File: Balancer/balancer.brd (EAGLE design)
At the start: 170 x 230 mm, 303 parts, among them Q1 BSS123W, Q10A SIR882DP-T1-GE3, Q10B SIS468DN-T1-GE3, Q11A SIR882DP-T1-GE3, Q11B SIS468DN-T1-GE3, Q12A SIR882DP-T1-GE3, Q12B SIS468DN-T1-GE3, Q1A8 SIR882DP-T1-GE3, Q1B8 SIS468DN-T1-GE3, Q2 BSS123W, Q3A SIR882DP-T1-GE3, Q3B SIS468DN-T1-GE3, Q4 MMBT3906LT1G, Q4A SIR882DP-T1-GE3, Q4B SIS468DN-T1-GE3, Q5 FDN5618P, Q5A SIR882DP-T1-GE3, Q5B SIS468DN-T1-GE3, Q6 CMPT3904E_TR_PBFREE, Q6A SIR882DP-T1-GE3, Q6B SIS468DN-T1-GE3, Q9A SIR882DP-T1-GE3, Q9B SIS468DN-T1-GE3, T10 750312504, T11 750312504, T12 750312504, T3 750312504, T4 750312504, T5 750312504, T6 750312504, T8 750312504, T9 750312504, U1 LTC3300ILXE-1PBF, U2 LTC3300ILXE-1PBF

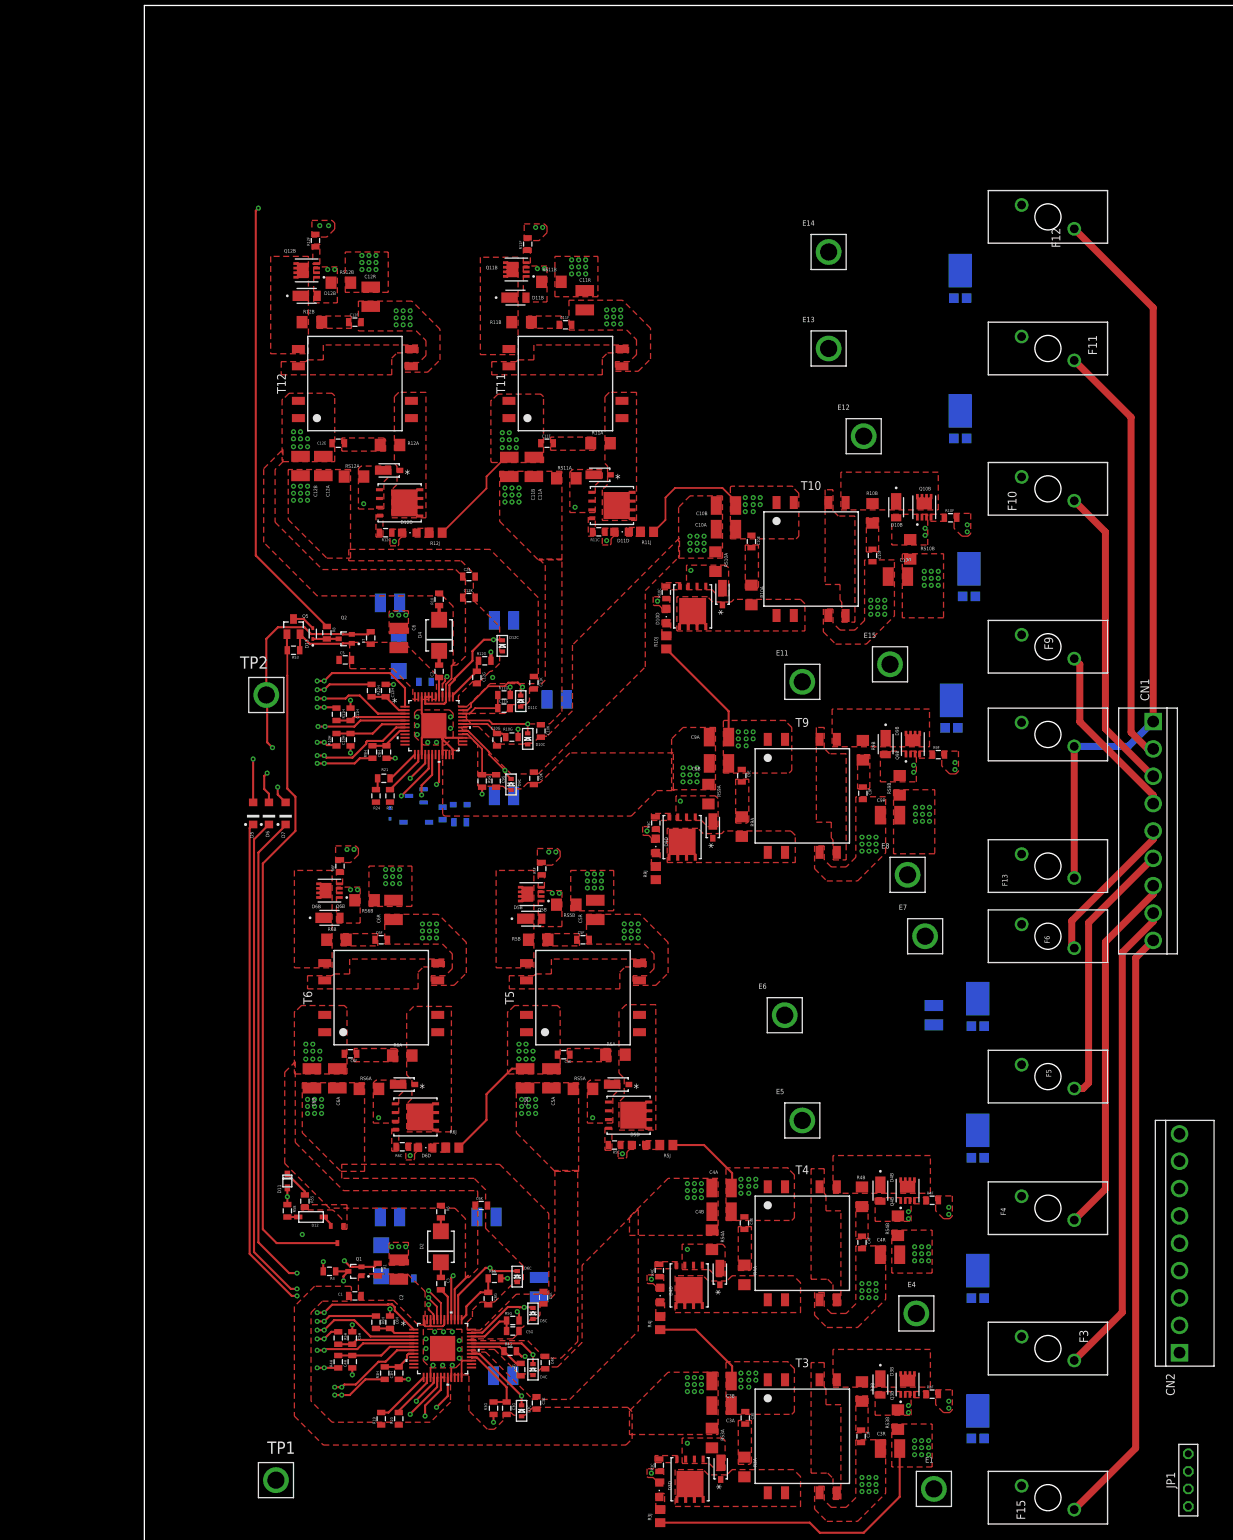
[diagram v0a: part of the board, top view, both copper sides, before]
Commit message: finished L3 and get half of L4 done
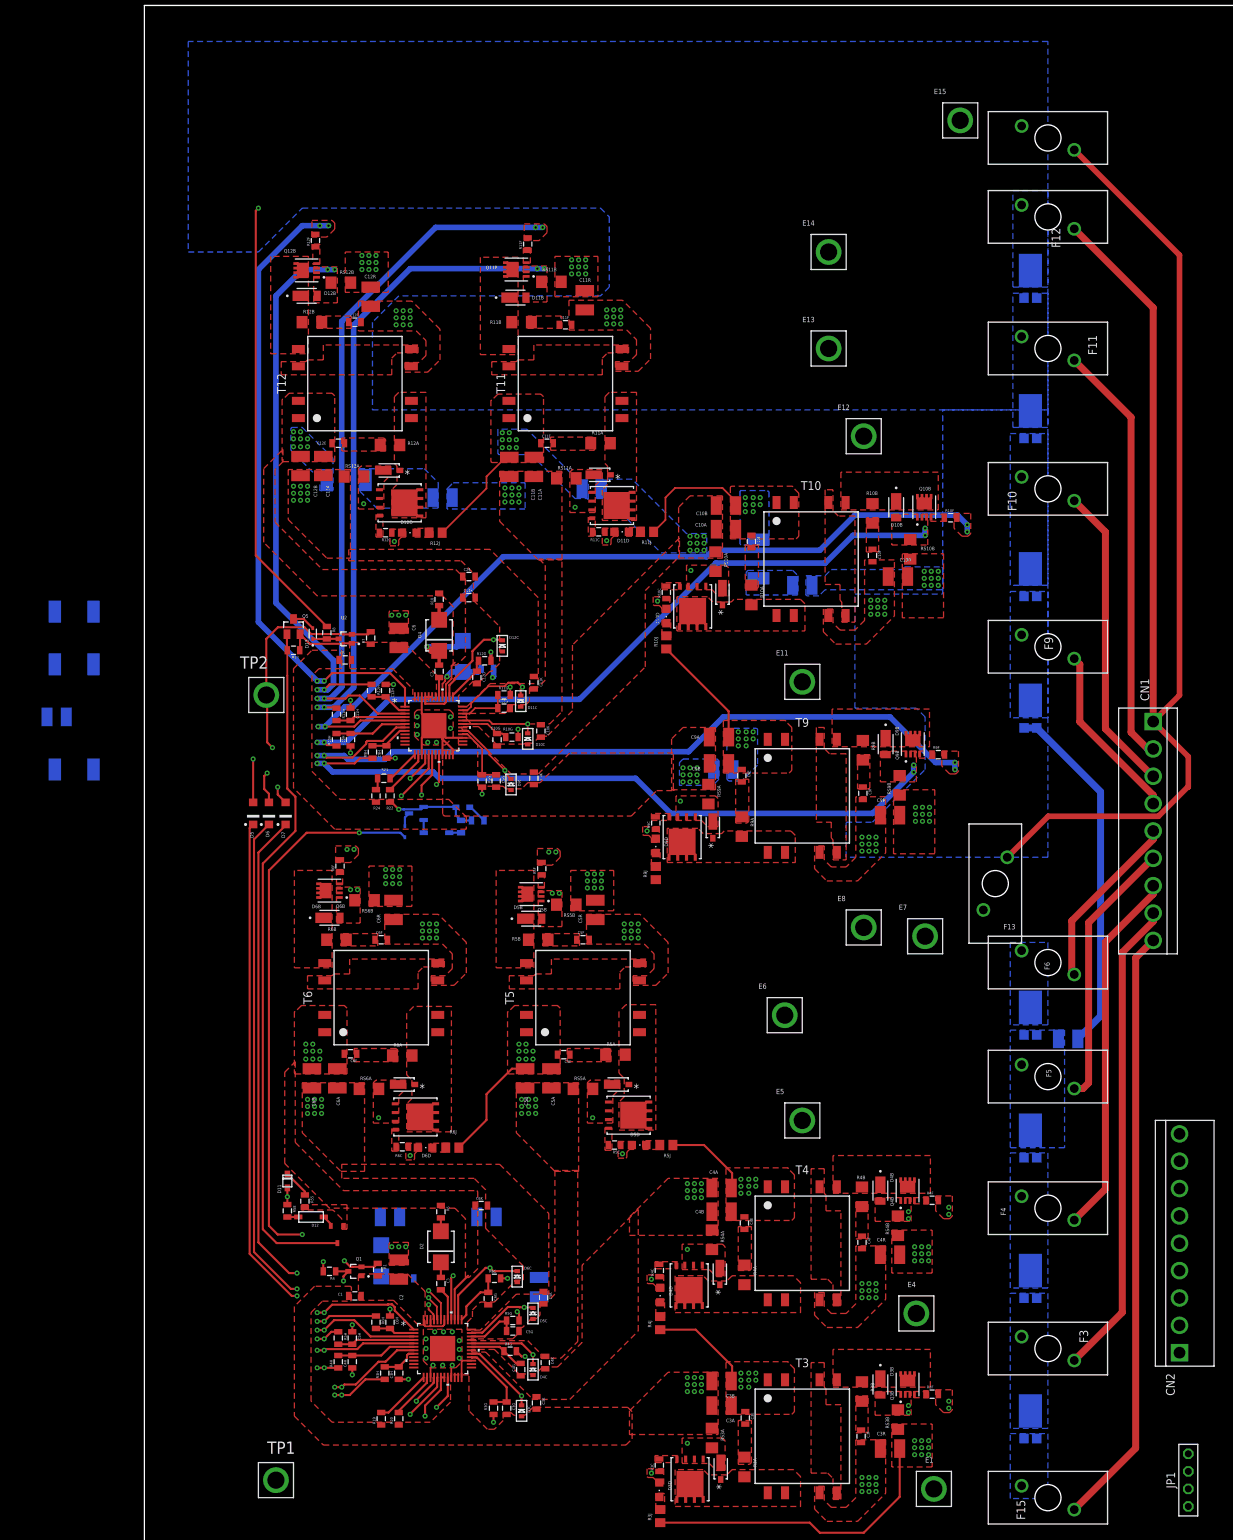
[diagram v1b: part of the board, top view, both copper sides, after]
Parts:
- added R11, R12, R13, R15, R16: 0, rcl:R2512
- moved C12 115.2 mm to (-12.7, 127.0)
- moved F14 86.4 mm to (130.8, 210.8)
- moved E15 79.4 mm to (118.1, 213.4)
- moved C17 39.2 mm to (95.2, 146.1), turned to 180 degrees
- moved C18 32.0 mm to (83.8, 119.4)
- moved C16 22.9 mm to (64.8, 160.0), turned to 180 degrees
- moved C13 19.7 mm to (133.7, 80.4), turned to 0 degrees
- moved C15 17.0 mm to (43.2, 158.8), turned to 180 degrees
- moved D9E 11.4 mm to (128.3, 128.3)
- moved D11E 10.2 mm to (128.3, 170.2)
- moved D12E 10.2 mm to (128.3, 190.5)
- moved E8 9.92 mm to (104.1, 96.5)
- moved D3 9.27 mm to (46.1, 135.8)
- moved C8 9.22 mm to (49.7, 134.0), turned to 180 degrees
- moved D10E 8.89 mm to (128.3, 147.3)
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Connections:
- net N$78 renamed C
- removed net C7: R54.1, R56.1
- new net N$66: C9.1, R11.1
- new net N$69: C11.1, R12.1
- new net N$71: C12.1, R13.1
- new net N$76: C15.1, R15.1
- new net N$92: C17.1, R16.1
- net C10: now also R16.2; no longer C17.1
- net C12: now also R15.2; no longer C15.1
- net C3: now also R13.2; no longer C12.1
- net C4: now also R12.2; no longer C11.1
- net C6: now also R11.2, R54.1, R56.1; no longer C9.1
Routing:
- net G10S: track 12.9 -> 120.2 mm
- net BAT+: track 108.0 -> 208.7 mm
- net N$100: track 3.01 -> 103.4 mm
- net G9S: track 14.8 -> 112.6 mm
- net N$84: track 8.31 -> 100.1 mm
- net G11S: track 14.0 -> 104.9 mm
- net N$116: track 2.84 -> 91.7 mm
- net N$5: track 17.0 -> 96.0 mm, vias 2 -> 3
- net G12S: track 16.8 -> 92.7 mm
- net N$132: track 8.19 -> 79.6 mm
- net C6: track 87.9 -> 150.0 mm, vias 67 -> 68
- net N$46: track 2.06 -> 9.64 mm, vias 0 -> 1
- net N$135: track 3.21 -> 8.62 mm
- net N$23: track 22.0 -> 25.8 mm
- net N$7: track 0.00 -> 2.85 mm
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- added copper zone on layer 16, net C10
- added copper zone on layer 16, net C11
- added copper zone on layer 16, net C12
- added copper zone on layer 16, net C3
- added copper zone on layer 16, net C4
- added copper zone on layer 16, net C5
- added copper zone on layer 16, net C6
- added copper zone on layer 16, net C9
- added copper zone on layer 16, net N$76
- added copper zone on layer 16, net N$92
- added copper zone on layer 16, net TOP6_TS
- added copper zone on layer 16, net V-

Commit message: Finished PCB drawing
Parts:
- removed C1A8, C1B8: 100uF, rcl:C1210
- removed C1E8, C1F8, C1H8: 470pF, Ilya_Teach:0805
- removed C1G8: 2.2nF, Ilya_Teach:0805
- removed C1R8: 2.2uF, rcl:C1210
- removed D1A8: DFLS260Q-7, balancer:SDO_POWERDI123_DIO
- removed D1B8: DFLS1100-7, DFLS1100-7:DIO_DFLS1100-7
- removed D1C8: (no value), adafruit:SOD-523
- removed D8E: SBR10U200P5, balancer:POWERDI5
- removed Q1A8: SIR882DP-T1-GE3, balancer:POWERPAK_SO-8_SINGLE_VIS
- removed Q1B8: SIS468DN-T1-GE3, SIS892DN:VISHAY_SIS468DN-T1-GE3
- removed R13: 0, rcl:R2512
- removed R1A8, R1B8: 20, rcl:R1206
- removed R1C8, R1F8: 5.1, Ilya_Teach:0805
- removed R1G8, R1H8: 20, Ilya_Teach:0805
- removed RS1A8: 0.005, rcl:R1206
- removed RS1B8: 0.01, rcl:R1206
- removed T8: 750312504, 750312504:WE-FLYLT_EP13_2381
- moved C12 132.5 mm to (81.8, 34.2)
- moved R12 130.5 mm to (87.6, 48.3), turned to 90 degrees
- moved R11 79.0 mm to (36.8, 78.7)
- moved C10 33.6 mm to (78.7, 71.1), turned to 270 degrees
- moved C11 23.2 mm to (79.6, 38.6)
- moved C9 19.4 mm to (45.7, 71.1), turned to 180 degrees
- moved D1 12.8 mm to (47.0, 47.0), turned to 90 degrees
- moved C4 12.0 mm to (49.5, 41.9), turned to 180 degrees
- moved C10R 0.38 mm to (109.1, 146.9)
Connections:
- removed net N$136: Q1A8.4, R1C8.2
- removed net N$137: D1C8.K, R1C8.1
- removed net N$138: C1A8.2, C1B8.2, C1G8.2, D1C8.A, D8E.P$2, D8E.P$3, RS1A8.1
- removed net N$139: C1E8.2, R1A8.1
- removed net N$140: C1A8.1, C1B8.1, C1E8.1, D8E.P$1, T8.1, T8.2
- removed net N$141: D1A8.1, Q1A8.5, Q1A8.6, Q1A8.7, Q1A8.8, Q1A8.9, R1A8.2, T8.10, T8.9
- removed net N$142: C1G8.1, R1G8.1
- removed net N$143: D1A8.2, Q1A8.1, Q1A8.2, Q1A8.3, R1G8.2, RS1A8.2
- removed net N$144: T8.4, T8.6
- removed net N$145: C1F8.1, R1B8.2
- removed net N$146: C1F8.2, C1R8.1, T8.7
- removed net N$147: D1B8.K, Q1B8.5, Q1B8.6, Q1B8.7, Q1B8.8, Q1B8.9, R1B8.1, T8.5
- removed net N$148: D1B8.A, Q1B8.1, Q1B8.2, Q1B8.3, R1H8.1, RS1B8.2
- removed net N$149: C1H8.2, R1H8.2
- removed net N$150: Q1B8.4, R1F8.1
- removed net N$151: R1F8.2
- removed net N$156: C1H8.1, C1R8.2, RS1B8.1
- removed net N$71: C12.1, R13.1
- net C3: now also C12.1; no longer R13.2
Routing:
- net G4S: track 14.4 -> 116.6 mm
- net N$36: track 3.05 -> 99.7 mm
- net G3S: track 13.7 -> 106.6 mm
- net G5S: track 15.6 -> 107.5 mm
- net N$20: track 8.18 -> 94.6 mm
- net N$52: track 3.47 -> 85.3 mm
- net G6S: track 16.3 -> 92.4 mm
- net N$68: track 8.83 -> 79.2 mm
- net C6: track 150.0 -> 204.6 mm
- net BOOST+: track 6.48 -> 12.8 mm
- net N$1: track 2.18 -> 8.09 mm, vias 0 -> 1
- net V-: track 102.7 -> 105.3 mm
- net C5: track 58.2 -> 59.7 mm, vias 18 -> 19
- added copper zone on layer 16, net BOT6_TS
- added copper zone on layer 1, net N$21
- added copper zone on layer 1, net N$38
- added copper zone on layer 16, net N$66
- added copper zone on layer 16, net N$69
- removed copper zone on layer 1, net N$110
- removed copper zone on layer 1, net N$87

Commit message: done final check, generated Gerber file
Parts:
- removed CN1, CN2: (no value), jst-vh:B9P-VH
- removed JP1: PINHD-1X4, Connector:1X04
- removed TP1, TP2: 2501-2-00-80-00-00-07-0, Turret:MILMAX_2501-2-00-80-00-00-07-0
- added BATT, VOLT_TAPS: (no value), jst-vh:B9P-VH
- added COMM: PINHD-1X4, Connector:1X04
- added WDTA, WDTC: 2501-2-00-80-00-00-07-0, Turret:MILMAX_2501-2-00-80-00-00-07-0
- moved D11E 10.5 mm to (118.1, 167.6)
- moved Q10B 10.5 mm to (102.7, 154.8)
- moved R16 10.5 mm to (78.7, 147.3)
- moved RS10A 10.5 mm to (72.5, 146.9)
- moved C3E 10.5 mm to (76.8, 23.0)
- moved D5E 10.5 mm to (118.1, 63.5)
- moved D9A 10.5 mm to (72.1, 108.5)
- moved D9E 10.5 mm to (118.1, 125.7)
- moved R4F 10.5 mm to (103.9, 54.5)
- moved R9B 10.5 mm to (93.9, 119.6)
- moved C11 10.5 mm to (69.5, 36.1)
- moved C9F 10.5 mm to (93.9, 113.4)
- moved D10E 10.5 mm to (118.1, 144.8)
- moved D12E 10.5 mm to (118.1, 188.0)
- moved D3D 10.5 mm to (64.4, 12.6)
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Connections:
- net BAT+: now also BATT.1; no longer CN1.1
- net C10: now also VOLT_TAPS.7; no longer CN2.7
- net C11: now also VOLT_TAPS.8; no longer CN2.8
- net C12: now also VOLT_TAPS.9; no longer CN2.9
- net C3: now also VOLT_TAPS.2; no longer CN2.2
- net C4: now also VOLT_TAPS.3; no longer CN2.3
- net C5: now also VOLT_TAPS.4; no longer CN2.4
- net C6: now also VOLT_TAPS.5; no longer CN2.5
- net C9: now also VOLT_TAPS.6; no longer CN2.6
- net CSBI: now also COMM.3; no longer JP1.3
- net N$14: now also BATT.2; no longer CN1.2
- net N$18: now also BATT.3; no longer CN1.3
- net N$22: now also BATT.4; no longer CN1.4
- net N$23: now also BATT.5; no longer CN1.5
- net N$25: now also BATT.6; no longer CN1.6
- net N$26: now also BATT.7; no longer CN1.7
- net N$28: now also BATT.8; no longer CN1.8
- net N$30: now also BATT.9; no longer CN1.9
- net SCKI: now also COMM.2; no longer JP1.2
- net SDIO: now also COMM.1; no longer JP1.1
- net V-: now also COMM.4, VOLT_TAPS.1; no longer CN2.1, JP1.4
- net WDTA: now also WDTA.1; no longer TP1.1
- net WDTC: now also WDTC.1; no longer TP2.1
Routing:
- net BAT+: track 208.7 -> 208.2 mm
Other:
- board size 170 x 230 mm -> 145 x 220 mm

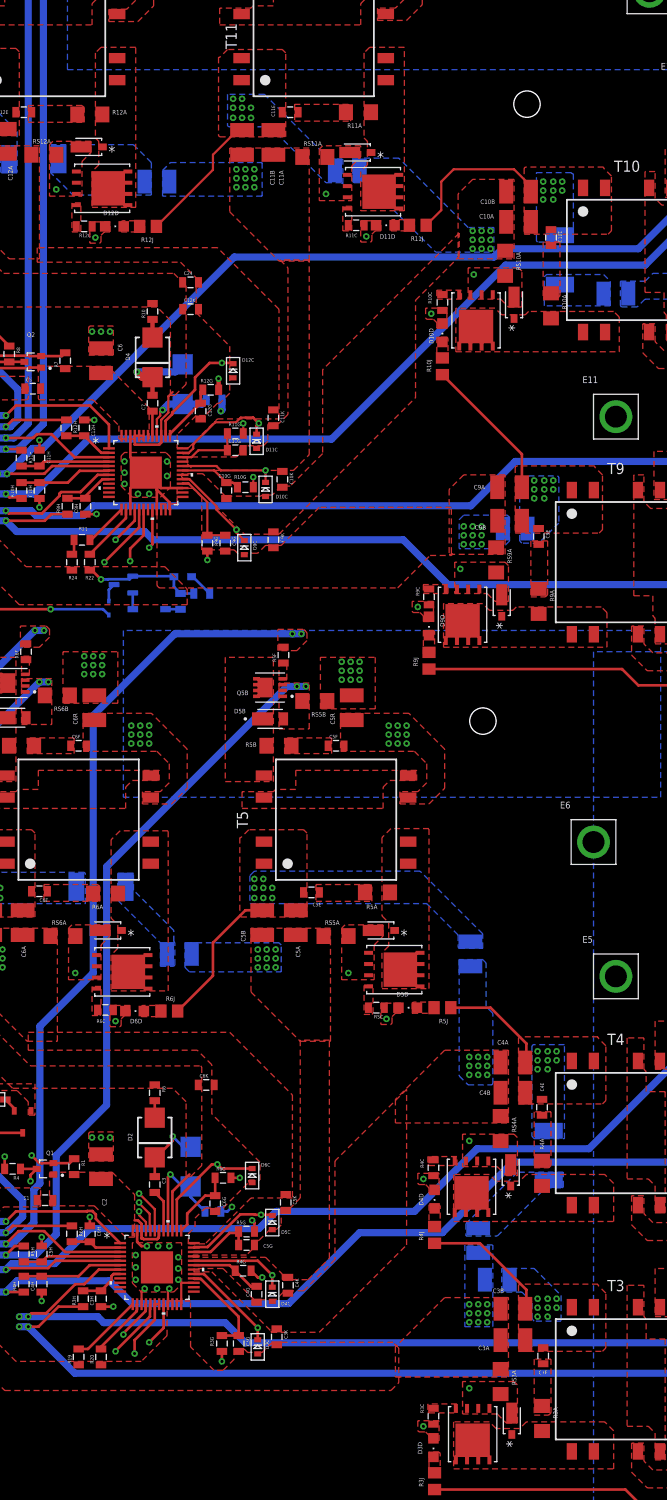
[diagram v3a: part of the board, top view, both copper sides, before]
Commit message: fixed wrong library on D3A-D12A
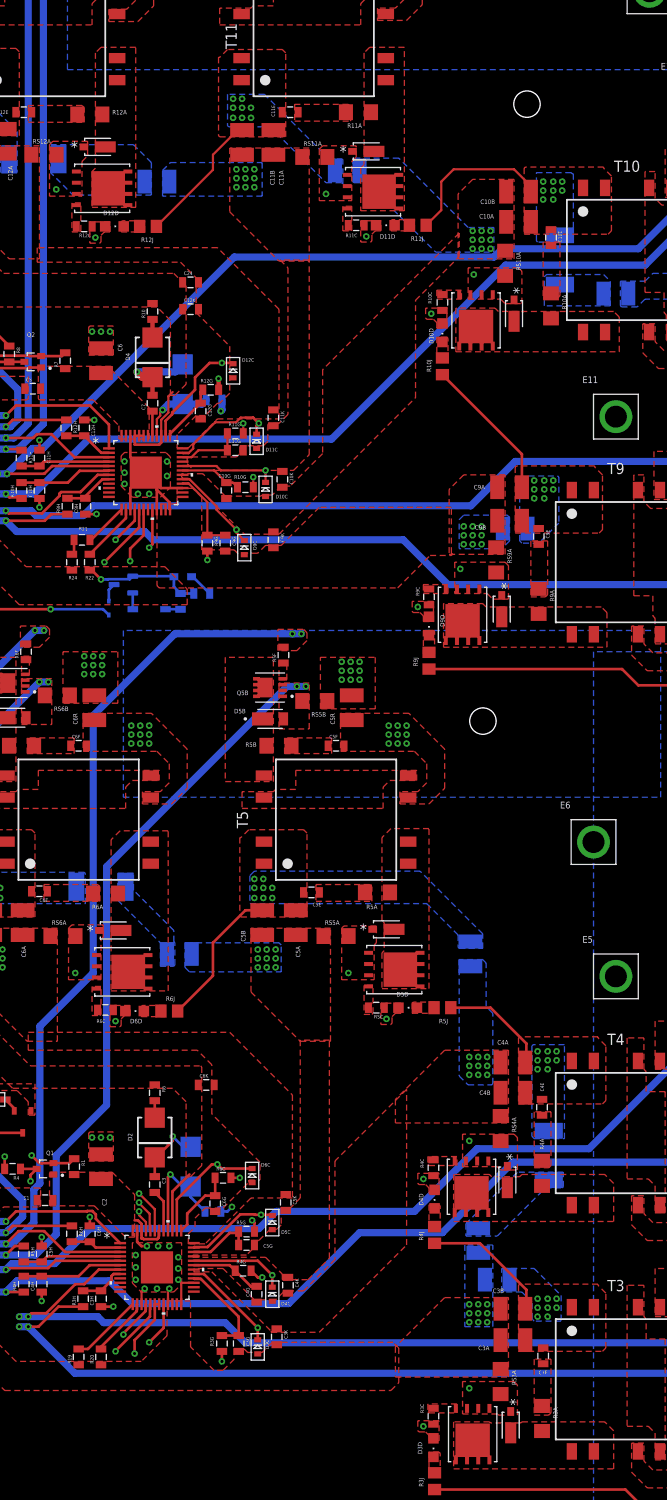
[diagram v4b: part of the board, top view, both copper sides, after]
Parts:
- moved D11A 1.02 mm to (56.8, 159.6), turned to 0 degrees
- moved D10A 1.02 mm to (73.5, 141.2), turned to 270 degrees
- moved D12A 1.02 mm to (26.3, 160.1), turned to 0 degrees
- moved D4A 0.97 mm to (72.8, 42.9), turned to 270 degrees
- moved D9A 0.76 mm to (72.1, 107.7), turned to 270 degrees
- moved D5A 0.65 mm to (59.1, 71.4), turned to 0 degrees
- moved D6A 0.64 mm to (28.1, 71.2), turned to 0 degrees
- moved D3A 0.52 mm to (73.2, 15.1), turned to 270 degrees
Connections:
- net N$109: now also D11A.2; no longer D11A.1
- net N$111: now also D11A.1; no longer D11A.2
- net N$125: now also D12A.2; no longer D12A.1
- net N$127: now also D12A.1; no longer D12A.2
- net N$15: now also D3A.2; no longer D3A.1
- net N$16: now also D3A.1; no longer D3A.2
- net N$29: now also D4A.2; no longer D4A.1
- net N$31: now also D4A.1; no longer D4A.2
- net N$45: now also D5A.2; no longer D5A.1
- net N$47: now also D5A.1; no longer D5A.2
- net N$61: now also D6A.2; no longer D6A.1
- net N$63: now also D6A.1; no longer D6A.2
- net N$77: now also D9A.2; no longer D9A.1
- net N$79: now also D9A.1; no longer D9A.2
- net N$93: now also D10A.2; no longer D10A.1
- net N$95: now also D10A.1; no longer D10A.2
